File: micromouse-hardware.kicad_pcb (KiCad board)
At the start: 2 copper layers, 51 parts, among them Q1 MBT3904DW1, Q2 MBT3904DW1, Q3 MBT3904DW1, Q4 TEFT4300, Q5 TEFT4300, Q6 TEFT4300, Q7 TEFT4300, Q8 TEFT4300, SW1 SLW-116641-5A-S-D, SW2 SW_DIP_x02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

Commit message: second commit
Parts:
- moved A1 38.9 mm to (132.1, 100.2), turned to 90 degrees
- moved U2 9.00 mm to (155.9, 74.4)
- moved U3 9.00 mm to (146.9, 74.4)
- moved ME1 6.29 mm to (148.5, 121.7)
- moved ME2 6.29 mm to (153.0, 121.7)
- moved R3 5.37 mm to (126.5, 81.5)
- moved R1 5.01 mm to (121.5, 81.5)
- moved R2 3.79 mm to (124.0, 81.5)
- moved C1 2.50 mm to (158.5, 107.0)
- moved C2 2.50 mm to (158.5, 109.5)
- moved C3 2.50 mm to (158.5, 111.5)
- moved R18 0.71 mm to (156.1, 58.0)
- moved R6 0.16 mm to (129.2, 67.0)
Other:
- board outline added: 85 x 103.5 mm

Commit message: before routing
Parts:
- added BT1: Battery_Cell, Connector_PinHeader_2.54mm:PinHeader_1x02_P2.54mm_Vertical, F.Cu at (157.0, 106.5)
- C1, C2, C3, C4, C5: footprint Capacitor_SMD:C_0201_0603Metric -> Capacitor_SMD:C_0603_1608Metric
- L1: value 220uH -> 22uH; footprint Inductor_SMD:L_0201_0603Metric -> Inductor_SMD:L_7.3x7.3_H3.5
- R1, R10, R11, R12, R13, R14, R15, R2, R21, R22, R3, R4, R5, R6, R7, R8, R9: footprint Resistor_SMD:R_0201_0603Metric -> Resistor_SMD:R_0603_1608Metric
- U2: value 74HC4051 -> CD74HC4051NSR; footprint Package_SO:SOIC-14-16_3.9x9.9mm_P1.27mm -> Package_SO:SOIC-16_4.55x10.3mm_P1.27mm
- moved R22 15.3 mm to (176.7, 93.0), turned to 180 degrees
- moved U4 13.9 mm to (178.4, 86.0)
- moved Q2 13.1 mm to (124.5, 70.8)
- moved C5 11.0 mm to (177.0, 98.5), turned to 180 degrees
- moved R21 9.54 mm to (181.0, 94.7), turned to 90 degrees
- moved C1 7.76 mm to (151.0, 105.0)
- moved C2 7.76 mm to (151.0, 107.5)
- moved C3 7.60 mm to (151.1, 110.0), turned to 180 degrees
- moved U1 7.22 mm to (144.1, 107.1)
- moved D6 7.07 mm to (181.0, 99.5)
- moved SW1 6.78 mm to (183.0, 103.5)
- moved R12 6.49 mm to (168.2, 63.5)
- moved R5 6.11 mm to (131.8, 69.0), turned to 0 degrees
- moved C4 5.92 mm to (190.2, 103.5)
- moved R4 5.69 mm to (131.8, 66.5), turned to 0 degrees
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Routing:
- net +5V: track 0.00 -> 316.0 mm, vias 0 -> 4
- net GND: track 0.00 -> 315.6 mm, vias 0 -> 5
- net Net-(Q5-E): track 0.00 -> 60.9 mm, vias 0 -> 1
- net Net-(Q7-E): track 0.00 -> 57.9 mm, vias 0 -> 1
- net Net-(A1-D13): track 0.00 -> 55.5 mm
- net /MUX_SEL_0: track 0.00 -> 50.6 mm
- net Net-(A1-D12): track 0.00 -> 49.5 mm
- net Net-(U3-Y4): track 0.00 -> 47.7 mm, vias 0 -> 3
- net /MUX_SEL_2: track 0.00 -> 46.7 mm
- net Net-(Q4-E): track 0.00 -> 40.7 mm, vias 0 -> 1
- net /MUX_SEL_1: track 0.00 -> 39.7 mm, vias 0 -> 1
- net Net-(U3-Y3): track 0.00 -> 36.5 mm, vias 0 -> 2
- net Net-(U3-Y2): track 0.00 -> 35.7 mm
- net Net-(SW1-A): track 0.00 -> 35.7 mm
- net Net-(ME2-M2): track 0.00 -> 33.8 mm
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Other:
- outline, holes or cut-outs redrawn

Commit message: nesto stabilno
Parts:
- added R23: 10K, Resistor_SMD:R_0603_1608Metric, F.Cu at (124.0, 103.8)
- added R24: 10K, Resistor_SMD:R_0603_1608Metric, F.Cu at (126.5, 103.8)
- D6: footprint Diode_SMD:D_0201_0603Metric -> Diode_SMD:D_0603_1608Metric_Pad1.05x0.95mm_HandSolder
- U2: value CD74HC4051NSR -> CD74HC4051M
- moved U3 2.50 mm to (145.0, 75.4)
- moved D6 1.00 mm to (181.0, 98.5)
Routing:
- net GND: track 315.6 -> 336.1 mm, vias 5 -> 3
- net /MUX_SEL_0: track 50.6 -> 33.1 mm
- net Net-(A1-D12): track 49.5 -> 63.0 mm
- net Net-(Q1B-B2): track 24.7 -> 12.1 mm
- net Net-(Q5-E): track 60.9 -> 72.3 mm, vias 1 -> 3
- net Net-(U3-Y4): track 47.7 -> 37.3 mm, vias 3 -> 2
- net Net-(U3-Y2): track 35.7 -> 26.4 mm
- net Net-(A1-D13): track 55.5 -> 63.3 mm, vias 0 -> 1
- net Net-(Q2B-C2): track 12.2 -> 19.7 mm, vias 0 -> 2
- net /MUX_SEL_2: track 46.7 -> 40.5 mm, vias 0 -> 2
- net Net-(U3-Y3): track 36.5 -> 32.1 mm
- net Net-(ME1-M1): track 23.1 -> 27.3 mm
- net Net-(SW1-A): track 35.7 -> 31.8 mm
- net Net-(ME2-M1): track 19.6 -> 23.0 mm, vias 0 -> 1
- net /D3: track 11.5 -> 14.6 mm
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
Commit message: before arduino rotae
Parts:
- moved C1 2.50 mm to (151.0, 107.5)
- moved C2 2.50 mm to (151.0, 105.0)
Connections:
- A1 pad 20: unconnected-(A1-A1-Pad20) -> /A1
- A1 pad 21: unconnected-(A1-A2-Pad21) -> /A2
- A1 pad 22: unconnected-(A1-A3-Pad22) -> /A3
- A1 pad 23: unconnected-(A1-A4-Pad23) -> /A4
- ME1 pad 3: /A0 -> /A1
- ME1 pad 4: /A1 -> /A2
- ME2 pad 3: /A2 -> /A4
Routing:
- net GND: track 336.1 -> 0.00 mm, vias 3 -> 0
- net +5V: track 313.2 -> 108.0 mm, vias 3 -> 1
- net /A1: track 0.00 -> 94.9 mm, vias 0 -> 1
- net /A2: track 0.00 -> 89.4 mm, vias 0 -> 1
- net Net-(Q5-E): track 72.3 -> 0.00 mm, vias 3 -> 0
- net /A3: track 0.00 -> 64.4 mm
- net Net-(A1-D13): track 63.3 -> 0.00 mm, vias 1 -> 0
- net Net-(A1-D12): track 63.0 -> 0.00 mm
- net /A4: track 0.00 -> 62.5 mm
- net Net-(Q7-E): track 60.4 -> 0.00 mm, vias 1 -> 0
- net Net-(Q4-E): track 40.8 -> 0.00 mm, vias 1 -> 0
- net Net-(Q6-E): track 34.5 -> 0.00 mm
- net Net-(U3-Y4): track 37.3 -> 3.00 mm, vias 2 -> 0
- net Net-(U3-Y3): track 32.1 -> 0.00 mm, vias 2 -> 0
- net /MUX_SEL_2: track 40.5 -> 9.42 mm, vias 2 -> 0
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
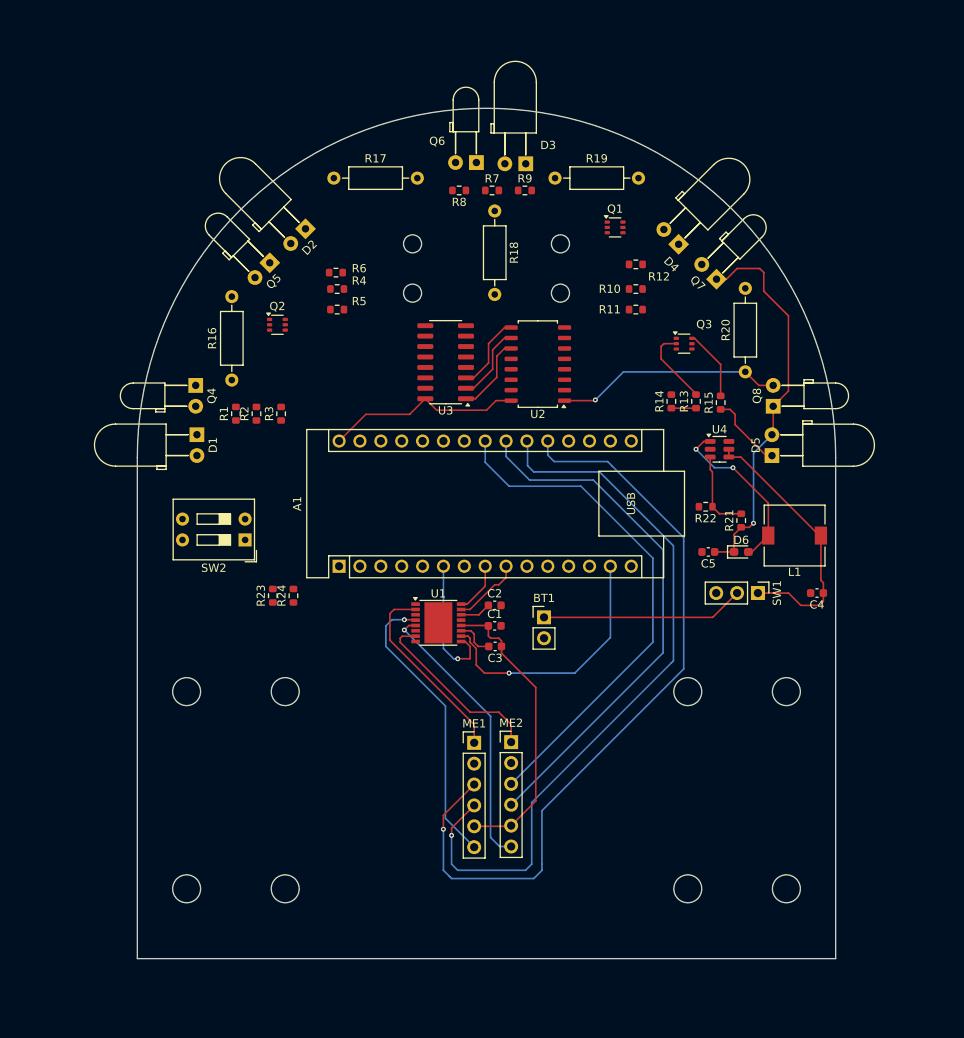
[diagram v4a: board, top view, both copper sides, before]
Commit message: everything except ground plane
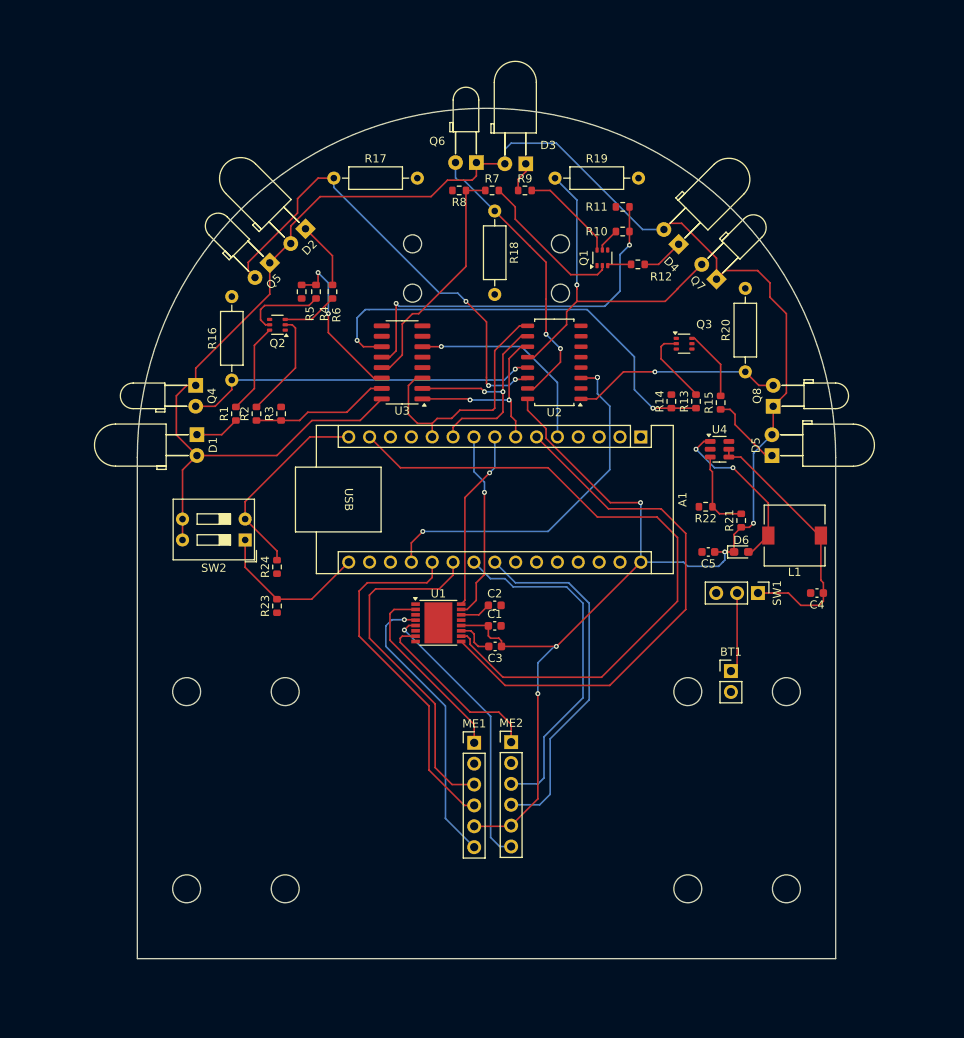
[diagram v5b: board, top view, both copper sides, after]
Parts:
- moved A1 40.0 mm to (168.8, 84.5), turned to -90 degrees
- moved BT1 23.7 mm to (179.8, 113.0)
- moved R11 12.6 mm to (166.6, 56.5)
- moved R10 7.18 mm to (166.6, 59.5)
- moved U3 5.30 mm to (139.7, 75.4)
- moved R5 4.84 mm to (127.5, 66.8), turned to -90 degrees
- moved R24 4.03 mm to (124.5, 100.3)
- moved Q1 4.01 mm to (164.1, 62.7), turned to 90 degrees
- moved R4 2.60 mm to (129.2, 66.8), turned to -90 degrees
- moved R6 2.36 mm to (131.2, 66.8), turned to -90 degrees
- moved U2 2.01 mm to (158.2, 75.4)
- moved R23 1.35 mm to (124.5, 105.1)
- moved R12 0.25 mm to (168.4, 63.5)
- turned Q2 to 180 degrees
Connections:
- ME1 pad 3: /A1 -> /A2
- ME1 pad 4: /A2 -> /A1
- ME2 pad 3: /A4 -> /A3
- ME2 pad 4: /A3 -> /A4
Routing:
- net +5V: track 108.0 -> 282.2 mm, vias 1 -> 5
- net Net-(Q5-E): track 0.00 -> 57.4 mm, vias 0 -> 3
- net Net-(U3-Y4): track 3.00 -> 55.0 mm, vias 0 -> 2
- net /D11: track 32.0 -> 82.9 mm, vias 1 -> 0
- net /A1: track 94.9 -> 44.0 mm, vias 1 -> 0
- net /D3: track 16.6 -> 65.7 mm, vias 1 -> 0
- net Net-(U3-Y3): track 0.00 -> 46.7 mm, vias 0 -> 2
- net /A2: track 89.4 -> 42.7 mm, vias 1 -> 0
- net /IRT_READ: track 0.00 -> 44.1 mm, vias 0 -> 3
- net Net-(Q7-E): track 0.00 -> 43.4 mm, vias 0 -> 1
- net Net-(Q4-E): track 0.00 -> 43.0 mm, vias 0 -> 1
- net Net-(Q6-E): track 0.00 -> 35.3 mm, vias 0 -> 2
- net Net-(U3-Y2): track 0.00 -> 29.2 mm
- net /LED_DEMUX_ENABLE: track 0.00 -> 24.9 mm, vias 0 -> 1
- net Net-(A1-D12): track 0.00 -> 24.6 mm
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
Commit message: Arduino Nano - Regulated 5V should be connected to 5V not VIN Moved some labels around to make connections more visible Placed No Connect Flags on all unused pins Added descriptive names to labels Changed the 5V regulator to LM2575GR-5.0 Made the Motor Driver use the battery voltage directly Re-routed some parts of the PCB to make space
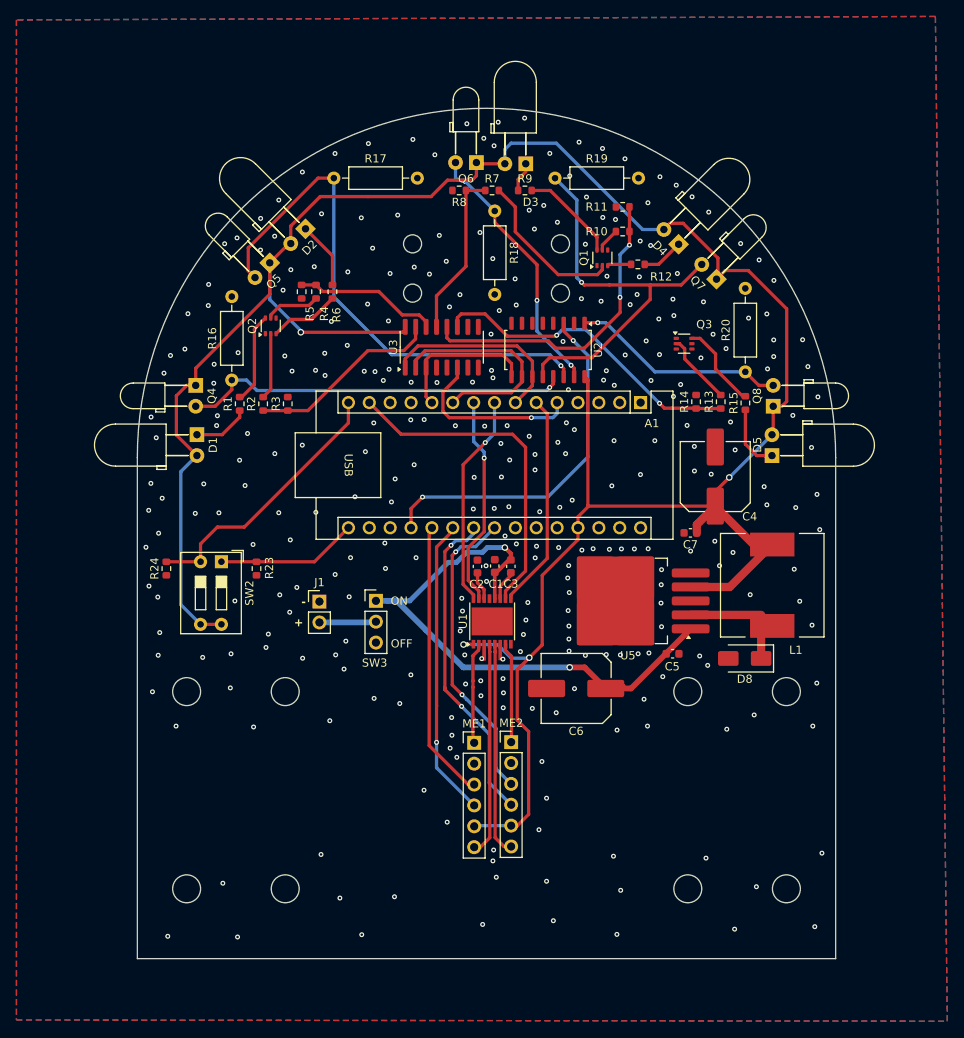
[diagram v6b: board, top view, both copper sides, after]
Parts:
- removed BT1: Battery_Cell, Connector_PinHeader_2.54mm:PinHeader_1x02_P2.54mm_Vertical
- removed D6: SS34, Diode_SMD:D_0603_1608Metric_Pad1.05x0.95mm_HandSolder
- removed R21: 110K, Resistor_SMD:R_0603_1608Metric
- removed R22: 15K, Resistor_SMD:R_0603_1608Metric
- removed SW1: SLW-116641-5A-S-D, Connector_PinHeader_2.54mm:PinHeader_1x03_P2.54mm_Vertical
- removed U4: MT3608, Package_TO_SOT_SMD:SOT-23-6
- added C6: 470uF, Capacitor_SMD:C_Elec_8x10.2, F.Cu at (160.9, 115.1)
- added C7: 100nF, Capacitor_SMD:C_0603_1608Metric, F.Cu at (174.8, 96.2)
- added D8: SS26, Diode_SMD:D_SMA, F.Cu at (181.4, 111.5)
- added J1: BATT-CONN, Connector_PinHeader_2.54mm:PinHeader_1x02_P2.54mm_Vertical, F.Cu at (129.7, 104.5)
- added SW3: SLW-116641-5A-S-D, Connector_PinHeader_2.54mm:PinHeader_1x03_P2.54mm_Vertical, F.Cu at (136.5, 104.5)
- added U5: LM2575GR-5.0, Package_TO_SOT_SMD:TO-263-5_TabPin3, F.Cu at (167.2, 104.5)
- C4: value 22uF X7R -> 470uF; footprint Capacitor_SMD:C_0603_1608Metric -> Capacitor_SMD:C_Elec_8x10.2
- C5: value 22uF X7R -> 100nF
- L1: value 22uH -> 220uH; footprint Inductor_SMD:L_7.3x7.3_H3.5 -> Inductor_SMD:L_12x12mm_H8mm
- moved C4 18.8 mm to (177.8, 89.3), turned to 90 degrees
- moved R24 13.5 mm to (111.0, 100.5)
- moved C5 13.1 mm to (172.7, 110.9), turned to 0 degrees
- moved C3 9.94 mm to (153.0, 100.2), turned to -90 degrees
- moved C1 7.29 mm to (151.0, 100.2), turned to 90 degrees
- moved L1 6.63 mm to (184.8, 102.5), turned to 90 degrees
- moved U1 6.55 mm to (150.7, 107.0), turned to 90 degrees
- moved R23 5.19 mm to (122.0, 100.5)
- moved C2 5.18 mm to (148.9, 100.3), turned to 90 degrees
- moved U3 5.17 mm to (144.6, 73.6), turned to 90 degrees
- moved A1 4.18 mm to (168.8, 80.3)
- moved SW2 3.92 mm to (117.7, 99.7), turned to -90 degrees
- moved R13 3.01 mm to (178.5, 80.2)
- moved R14 3.01 mm to (175.5, 80.2)
- moved R15 3.01 mm to (181.5, 80.4)
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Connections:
- net /D11 renamed /M2-IN2
- net /D3 renamed /M2-IN1
- net /D5 renamed /M1-IN1
- net /D6 renamed /M1-IN2
- A1 pad 20: /A1 -> /M1-C1
- A1 pad 21: /A2 -> /M1-C2
- A1 pad 22: /A3 -> /M2-C2
- A1 pad 23: /A4 -> /M2-C1
- A1 pad 27: unconnected-(A1-+5V-Pad27) -> +5V
- A1 pad 30: +5V -> unconnected-(A1-VIN-Pad30)
- C1 pad 1: +5V -> +VBAT
- C3 pad 1: +5V -> +VBAT
- C4 pad 1: Net-(SW1-A) -> +5V
- C5 pad 1: +5V -> +VBAT
- L1 pad 1: Net-(SW1-A) -> Net-(D8-K)
- L1 pad 2: Net-(D6-A) -> +5V
- ME1 pad 3: /A2 -> /M1-C1
- ME1 pad 4: /A1 -> /M1-C2
- ME2 pad 3: /A3 -> /M2-C1
- ME2 pad 4: /A4 -> /M2-C2
- Q3 pad 3: (no net) -> GND
- Q3 pad 4: (no net) -> GND
- Q3 pad 5: (no net) -> GND
- U1 pad 12: +5V -> +VBAT
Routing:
- net +VBAT: track 0.00 -> 72.2 mm, vias 0 -> 2
- net /A4: track 44.1 -> 0.00 mm
- net /A1: track 44.0 -> 0.00 mm
- net /A3: track 42.9 -> 0.00 mm
- net /A2: track 42.7 -> 0.00 mm
- net /M2-IN2: track 82.9 -> 40.7 mm
- net /M2-C2: track 0.00 -> 39.5 mm, vias 0 -> 2
- net /M2-IN1: track 65.7 -> 26.2 mm
- net /M2-C1: track 0.00 -> 37.3 mm, vias 0 -> 2
- net /M1-C2: track 0.00 -> 36.5 mm, vias 0 -> 1
- net /M1-C1: track 0.00 -> 34.1 mm
- net Net-(SW1-A): track 33.0 -> 0.00 mm
- net +5V: track 282.2 -> 306.2 mm, vias 5 -> 4
- net Net-(D6-A): track 20.5 -> 0.00 mm, vias 2 -> 0
- net Net-(U3-Y4): track 55.0 -> 39.1 mm
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- added copper zone on B.Cu, net GND
- added copper zone on F.Cu, net GND

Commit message: Change the transistor footprint, changed spacing around the components to allow for mounting hardware to be added
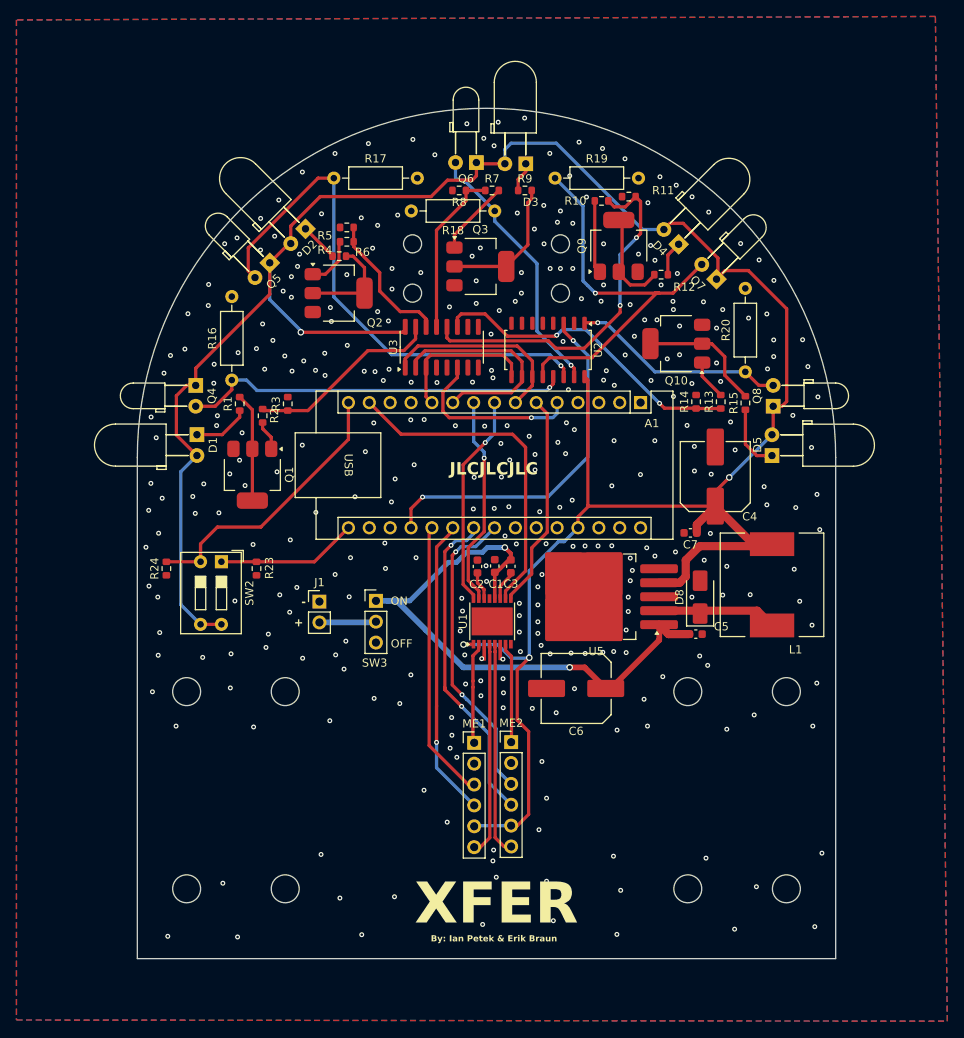
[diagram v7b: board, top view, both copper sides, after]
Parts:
- added Q10: BCP56, Custom:SOT-223-3_TabPin4, F.Cu at (173.1, 73.2)
- added Q9: BCP56, Custom:SOT-223-3_TabPin4, F.Cu at (166.1, 61.2)
- Q1, Q2, Q3: value MBT3904DW1 -> BCP56; footprint Package_TO_SOT_SMD:SOT-363_SC-70-6 -> Custom:SOT-223-3_TabPin4
- moved Q1 50.1 mm to (121.5, 89.1), turned to -90 degrees
- moved Q3 26.5 mm to (149.2, 63.8)
- moved R5 9.56 mm to (133.0, 59.0), turned to 180 degrees
- moved D8 9.23 mm to (176.0, 104.0), turned to 90 degrees
- moved Q2 9.17 mm to (132.0, 67.0), turned to 0 degrees
- moved R4 7.14 mm to (133.0, 60.8), turned to 180 degrees
- moved R10 4.53 mm to (164.0, 55.8)
- moved R6 4.40 mm to (132.1, 62.5), turned to 0 degrees
- moved U5 3.88 mm to (163.3, 104.0)
- moved C5 3.70 mm to (175.5, 108.5)
- moved R12 3.09 mm to (171.2, 64.8)
- moved R11 1.46 mm to (167.3, 55.2)
- moved R2 1.46 mm to (122.8, 81.9), turned to -90 degrees
- moved L1 0.06 mm to (184.8, 102.5)
- turned R18 to 180 degrees
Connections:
- Q1 pad 1: GND -> Net-(Q1-B)
- Q1 pad 2: Net-(Q1A-B1) -> Net-(Q1-C-Pad2)
- Q1 pad 3: Net-(Q1B-C2) -> GND
- Q1 pad 4: GND -> Net-(Q1-C-Pad2)
- Q2 pad 1: GND -> Net-(Q2-B)
- Q2 pad 2: Net-(Q2A-B1) -> Net-(Q2-C-Pad2)
- Q2 pad 3: Net-(Q2B-C2) -> GND
- Q2 pad 4: GND -> Net-(Q2-C-Pad2)
- Q3 pad 1: GND -> Net-(Q3-B)
- Q3 pad 2: Net-(Q3A-B1) -> Net-(Q3-C-Pad2)
- Q3 pad 4: GND -> Net-(Q3-C-Pad2)
- R1 pad 2: Net-(Q2A-C1) -> Net-(Q1-C-Pad2)
- R10 pad 2: Net-(Q1B-B2) -> Net-(Q9-B)
- R12 pad 2: Net-(Q1B-C2) -> Net-(Q9-C-Pad2)
- R13 pad 2: Net-(Q3A-B1) -> Net-(Q10-B)
- R15 pad 2: Net-(Q3A-C1) -> Net-(Q10-C-Pad2)
- R2 pad 2: Net-(Q2A-B1) -> Net-(Q1-B)
- R4 pad 2: Net-(Q2B-B2) -> Net-(Q2-B)
- R6 pad 2: Net-(Q2B-C2) -> Net-(Q2-C-Pad2)
- R7 pad 2: Net-(Q1A-B1) -> Net-(Q3-B)
- R9 pad 2: Net-(Q1A-C1) -> Net-(Q3-C-Pad2)
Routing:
- net Net-(Q1A-B1): track 19.4 -> 0.00 mm
- net Net-(Q3-C-Pad2): track 0.00 -> 16.8 mm
- net Net-(Q10-C-Pad2): track 0.00 -> 15.5 mm
- net Net-(Q1-C-Pad2): track 0.00 -> 13.2 mm
- net Net-(Q2-C-Pad2): track 0.00 -> 12.2 mm
- net Net-(Q1A-C1): track 11.9 -> 0.00 mm
- net Net-(Q9-C-Pad2): track 0.00 -> 11.3 mm
- net Net-(Q2A-C1): track 11.1 -> 0.00 mm
- net Net-(Q3A-C1): track 10.5 -> 0.00 mm
- net Net-(Q3-B): track 0.00 -> 9.19 mm
- net Net-(Q9-B): track 0.00 -> 8.89 mm
- net Net-(Q3A-B1): track 8.71 -> 0.00 mm
- net Net-(Q2B-C2): track 8.63 -> 0.00 mm
- net Net-(Q2A-B1): track 8.10 -> 0.00 mm
- net Net-(Q2B-B2): track 6.72 -> 0.00 mm
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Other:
- board text added: "By: Ian Petek & Erik Braun"
- board text added: "JLCJLCJLC"
- board text added: "XFER"
